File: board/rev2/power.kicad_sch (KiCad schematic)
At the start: 12 parts, among them J1 USB_C_Receptacle_USB2.0_14P, J2 Screw_Terminal_01x02, U2 TPSM53602RDA

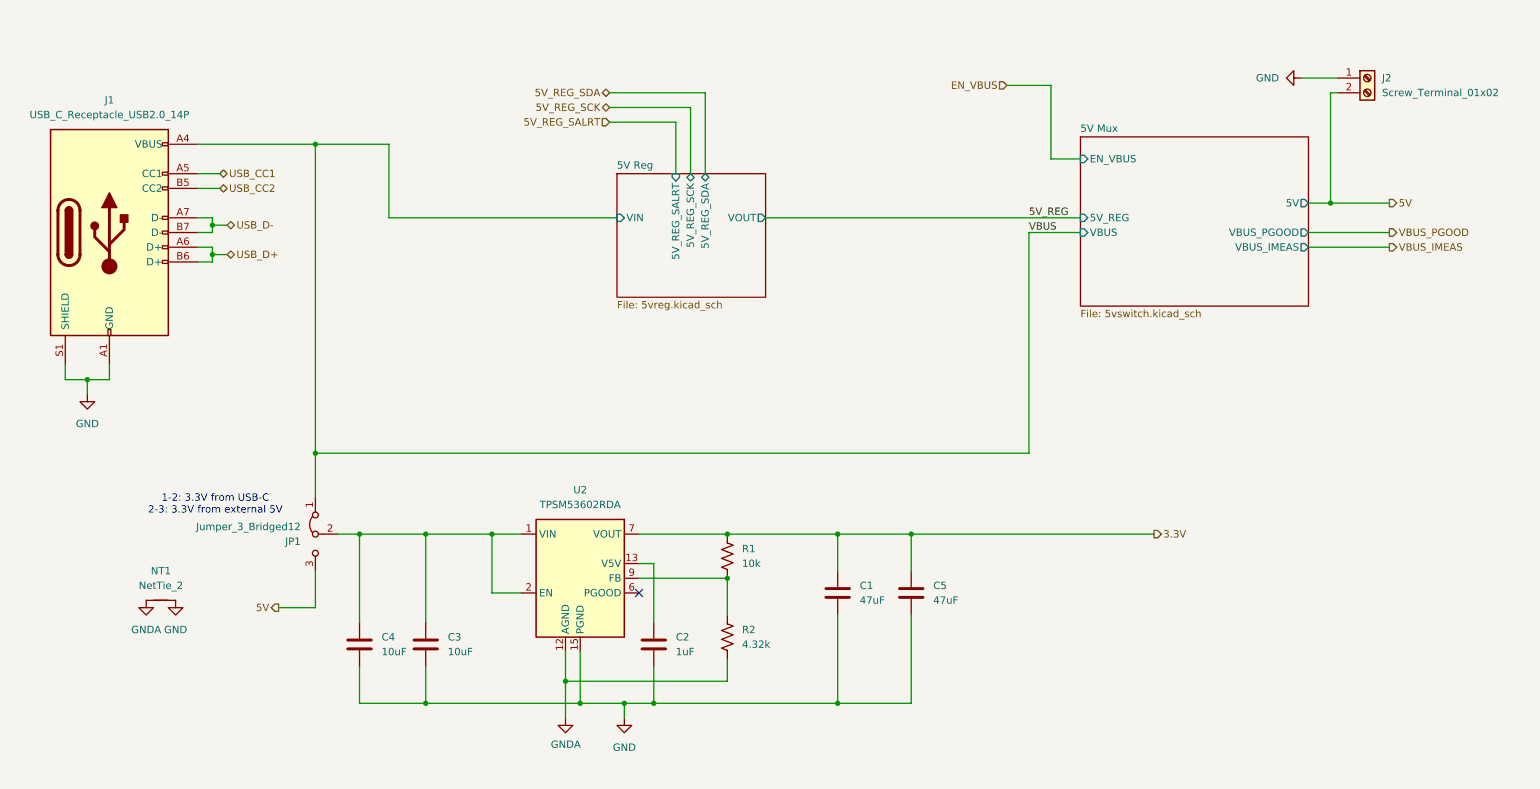
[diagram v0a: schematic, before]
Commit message: Finish most of power section of rev2 PCB
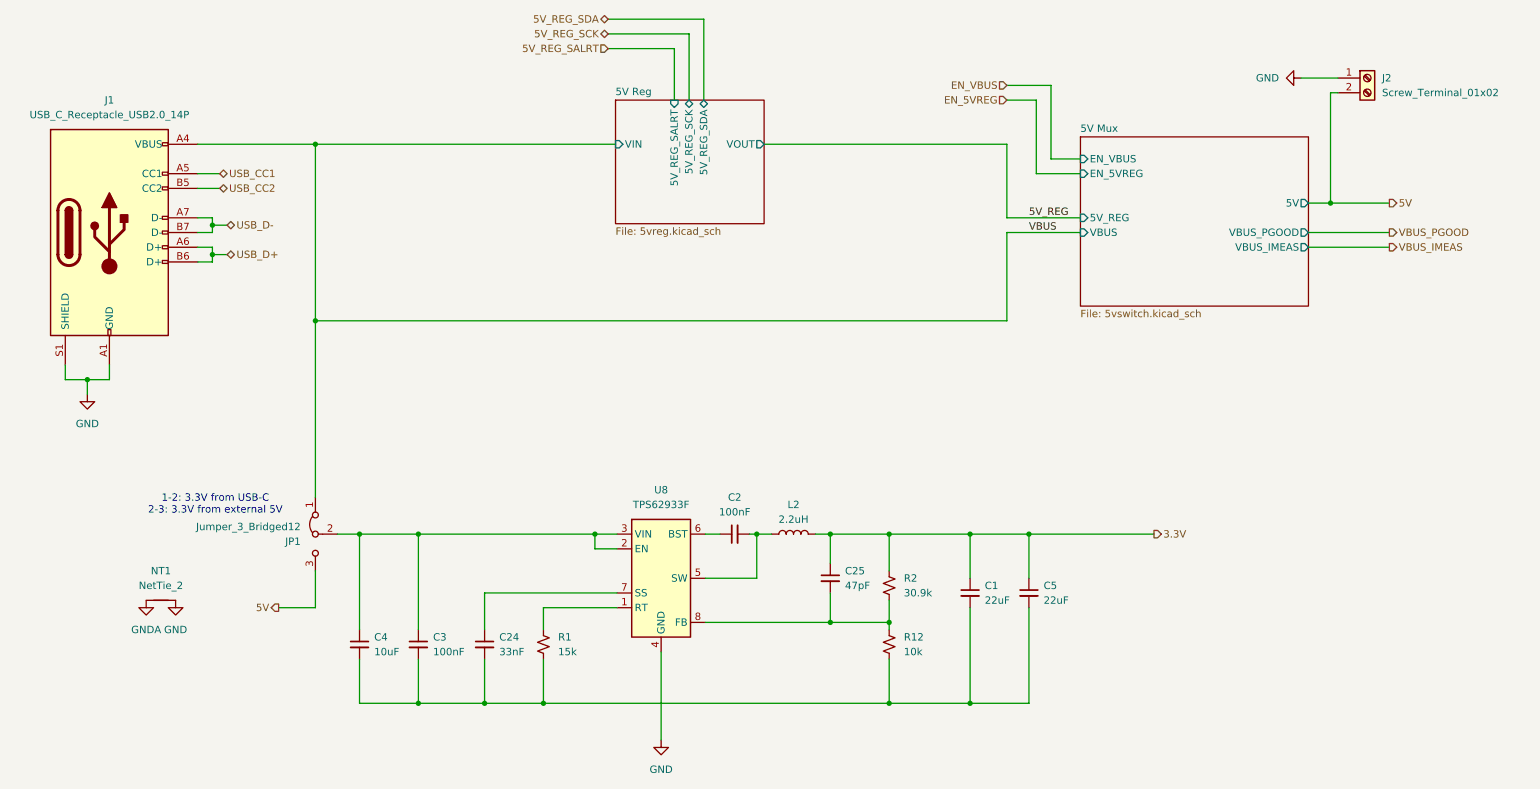
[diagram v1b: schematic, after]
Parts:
- removed C2: 1uF, symbol Device:C
- removed R1: 10k, symbol Device:R_US
- removed R2: 4.32k, symbol Device:R_US
- removed U2: TPSM53602RDA, Package_DFN_QFN:Texas_B3QFN-14-1EP_5x5.5mm_P0.65mm_ThermalVia, symbol Converter_DCDC:TPSM53602RDA
- added C2: 100nF, symbol Device:C_Small
- added C24: 33nF, symbol Device:C_Small
- added C25: 47pF, symbol Device:C_Small
- added L2: 2.2uH, symbol Device:L
- added R1: 15k, symbol Device:R_Small_US
- added R12: 10k, symbol Device:R_Small_US
- added R2: 30.9k, symbol Device:R_Small_US
- added U8: TPS62933F, Package_TO_SOT_SMD:SOT-583-8, symbol Regulator_Switching:TPS62933F
- C1, C5: value 47uF -> 22uF; symbol Device:C -> Device:C_Small
- C3: value 10uF -> 100nF; symbol Device:C -> Device:C_Small
- C4: symbol Device:C -> Device:C_Small
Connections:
- net 3.3V: now also C25.1, L2.2, R2.1
- net GND: now also U8.4 (GND); no longer C1.2, C3.2, C4.2, C5.2
- net at C3.1, C4.1, JP1.2 (C): now also U8.2 (EN), U8.3 (VIN)
- new net: C1.2, C24.2, C3.2, C4.2, C5.2, R1.2, R12.2
- new net: C2.1, U8.6 (BST)
- new net: C2.2, L2.1, U8.5 (SW)
- new net: R1.1, U8.1 (RT)
- new net: C24.1, U8.7 (SS)
- new net: C25.2, R12.1, R2.2, U8.8 (FB)
- no-connect marks 1 -> 0
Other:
- sheet 5V Mux ports: added EN_5VREG; removed none
- moved on the sheet: C1, C3, C5
